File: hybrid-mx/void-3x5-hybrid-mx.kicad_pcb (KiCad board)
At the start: 2 copper layers, 140.5 x 112.5 mm, 81 parts, among them J1 Conn_01x02, J2 Conn_01x03_MountingPin, J3 Conn_01x02

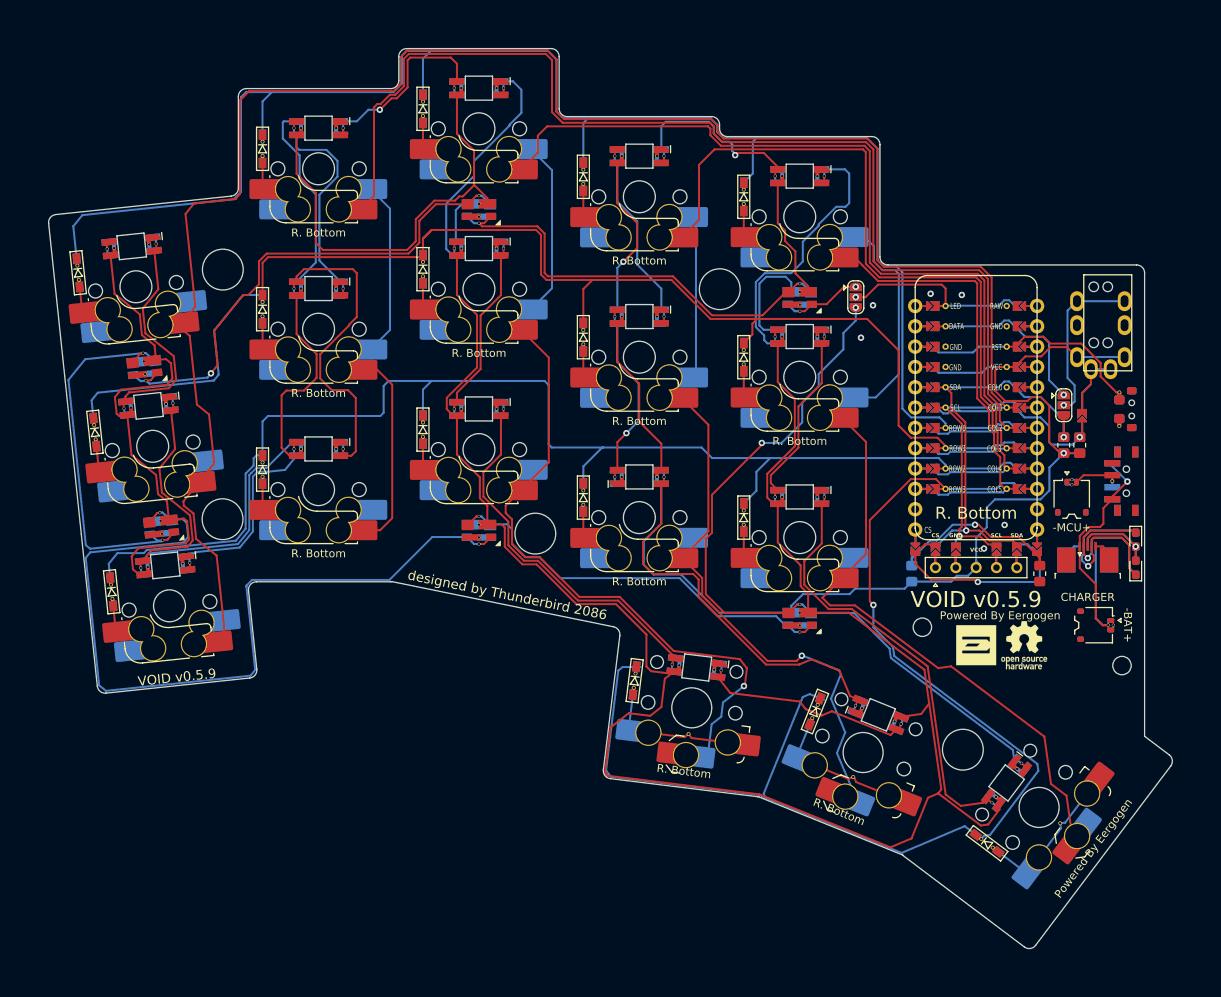
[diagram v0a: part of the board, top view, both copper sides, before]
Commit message: usb-c mod for hybrid
* updated
  - submodule
  - ergogen yaml
  - schematic and pcb
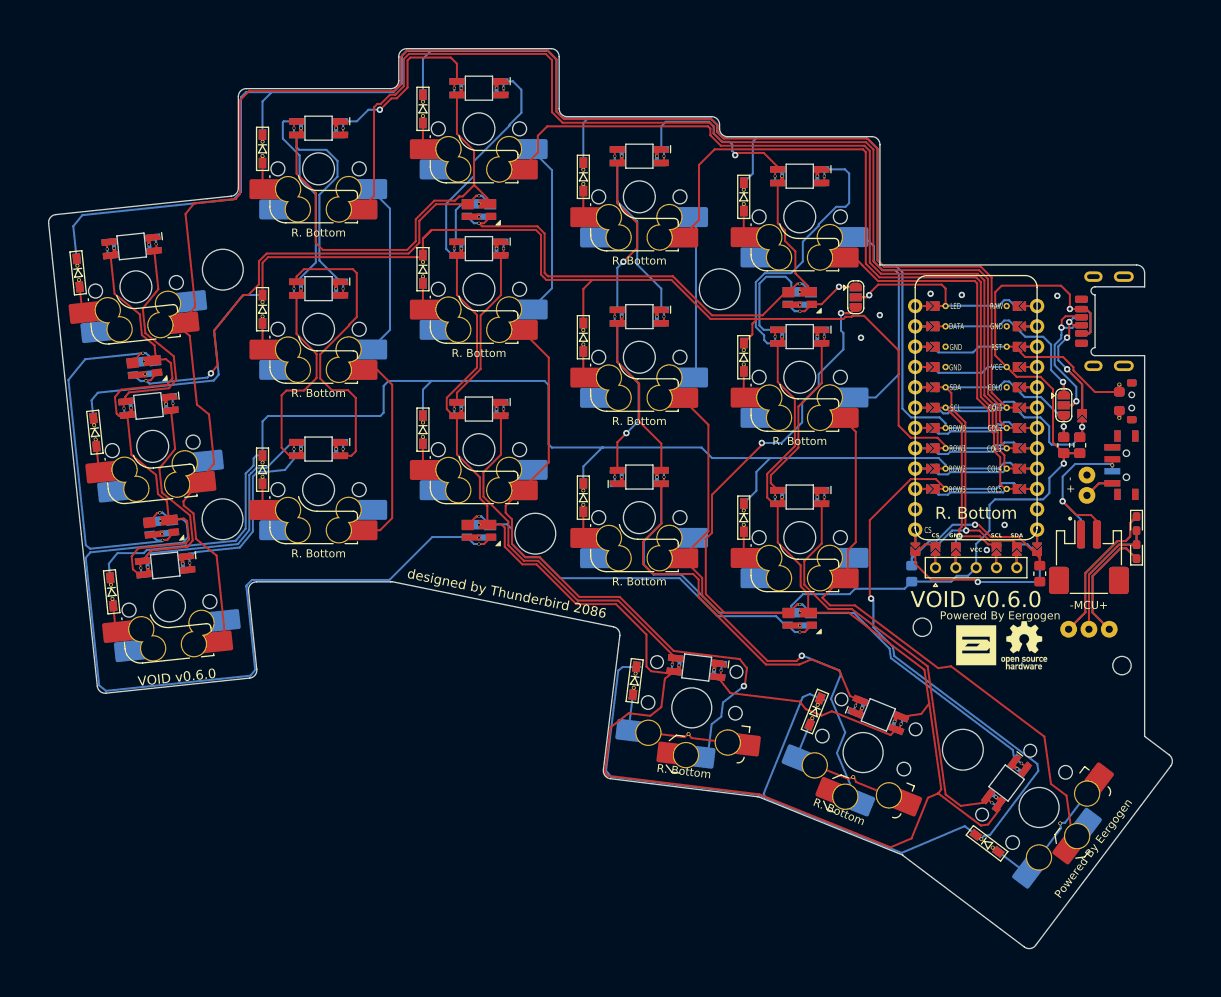
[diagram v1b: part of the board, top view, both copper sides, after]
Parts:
- removed TRRS1: MJ-4PP-9, TB2086_MISC:TRRS-PJ-320A-rev
- added J4: Conn_01x03, TB2086_MISC:Pogopin_1x03_P2.54mm, F.Cu at (210.9, 112.9)
- added SW_SPDT2: SW_SPDT2, TB2086_SMD:SW_SPDT_PCM12, F.Cu at (215.3, 92.4)
- J1: value Conn_01x02 -> USB_C_Receptacle_PowerOnly_6P; footprint TB2086_MISC:Molex_Pico-EZmate_78171-0002_1x02-1MP_P1.20mm_Vertical_rev -> TB2086_SMD:USB-20C-F-6C16_rev
- J2: value Conn_01x03_MountingPin -> Conn_01x02; footprint TB2086_MISC:TE_0-1734839-5_1x05-1MP_P0.5mm_Horizontal-rev -> TB2086_SMD:JST_PH_S2B-PH-SM4-TB_1x02-1MP_P2.00mm_Horizontal_rev
- J3: footprint TB2086_MISC:Molex_Pico-EZmate_78171-0002_1x02-1MP_P1.20mm_Vertical_rev -> TB2086_MISC:Pogopin_1x02_P2.54mm; moved to F.Cu
- L19, L20, L21, L22, L23, L24: footprint LED_SK6812MINI_PLCC4_3.5x3.5mm_P1.75mm_rev_all -> TB2086_LED:LED_SK6812MINI_PLCC4_3.5x3.5mm_P1.75mm_rev_all; moved to F.Cu
- LED1, LED2, LED3, LED4: footprint TB2086_SMD:LED_0603_1608Metric_Pad1.05x0.95mm_HandSolder -> TB2086_LED:LED_0603_1608Metric_Pad1.05x0.95mm_HandSolder
- R1: footprint R_0805_2012Metric_Pad1.20x1.40mm_HandSolder -> Resistor_SMD:R_0805_2012Metric_Pad1.20x1.40mm_HandSolder; moved to B.Cu
- R2: footprint R_0805_2012Metric_Pad1.20x1.40mm_HandSolder -> Resistor_SMD:R_0805_2012Metric_Pad1.20x1.40mm_HandSolder
- S16, S17: value SW_MX_HS -> SW_CHOC_HS
- S18: value SW_MX_HS -> SW_CHOC_HS; footprint TB2086_KEYSWITCH:SW_choc_v1_v2_HS_1.5u_reversible -> TB2086_KEYSWITCH:SW_choc_v1_v2_HS_1u_reversible
- SW_SPDT1: value SW_SPDT -> SW_SPDT1; footprint TB2086_SMD:SW_SPDT_PCM12_reversible -> TB2086_SMD:SW_SPDT_PCM12
- moved J1 22.7 mm to (214.5, 74.4), turned to 90 degrees
- moved J3 17.5 mm to (210.7, 94.9), turned to -90 degrees
- moved LED1 5.49 mm to (216.9, 99.7), turned to -90 degrees
- moved LED3 2.00 mm to (216.9, 103.2), turned to 90 degrees
- moved LED2 2.00 mm to (216.9, 99.7)
- moved SW_SPDT1 1.99 mm to (215.3, 92.4)
- moved LED4 1.51 mm to (216.9, 103.2)
- moved RSW1 0.99 mm to (216.3, 84.4)
- moved J2 0.15 mm to (210.9, 103.9)
- turned L19 to 0 degrees
- turned L23 to 0 degrees
- turned L24 to 0 degrees
- turned L20 to 0 degrees
- turned L21 to 6 degrees
- turned L22 to 6 degrees
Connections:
- J2 pad 1: BAT -> GND
- JP2 pad 2: Net-(JP2-C) -> Net-(J1-CC2)
- JP3 pad 2: Net-(JP3-B) -> Net-(J1-CC1)
- LED1 pad 1: Net-(J2-Pin_4) -> Net-(J4-Pin_1)
- LED1 pad 2: Net-(J2-Pin_3) -> Net-(J4-Pin_2)
- LED2 pad 1: Net-(J2-Pin_4) -> Net-(J4-Pin_1)
- LED2 pad 2: Net-(J2-Pin_3) -> Net-(J4-Pin_2)
- LED3 pad 1: Net-(J2-Pin_2) -> Net-(J4-Pin_3)
- LED3 pad 2: Net-(J2-Pin_3) -> Net-(J4-Pin_2)
- LED4 pad 1: Net-(J2-Pin_2) -> Net-(J4-Pin_3)
- LED4 pad 2: Net-(J2-Pin_3) -> Net-(J4-Pin_2)
- RSW1 pad MP: (no net) -> GND
- SW_SPDT1 pad 2: Net-(J1-Pin_2) -> Net-(J2-Pin_2)
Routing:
- net Net-(J4-Pin_1): track 0.00 -> 36.4 mm
- net Net-(J4-Pin_2): track 0.00 -> 32.2 mm
- net Net-(J4-Pin_3): track 0.00 -> 30.0 mm
- net BAT: track 37.1 -> 7.60 mm, vias 1 -> 0
- net Net-(J2-Pin_4): track 23.9 -> 0.00 mm, vias 1 -> 0
- net Net-(J1-CC1): track 0.00 -> 22.2 mm, vias 0 -> 3
- net Net-(JP2-C): track 20.9 -> 0.00 mm, vias 1 -> 0
- net Net-(J1-CC2): track 0.00 -> 20.5 mm, vias 0 -> 2
- net Net-(J2-Pin_3): track 19.3 -> 0.00 mm, vias 1 -> 0
- net VCC: track 627.1 -> 642.9 mm, vias 2 -> 3
- net Net-(JP3-B): track 13.8 -> 0.00 mm
- net GND: track 5.73 -> 0.00 mm, vias 6 -> 7
- net Net-(J1-Pin_2): track 4.83 -> 0.00 mm
- net LED_PER_KEY: track 93.4 -> 96.5 mm
- net LED_UNDERGLOW: track 10.1 -> 12.2 mm
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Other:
- outline, holes or cut-outs redrawn
- board text added: "- +"
- board text added: "VOID v0.6.0"
- board text removed: "-BAT+"
- board text removed: "CHARGER"
- board text removed: "VOID v0.5.9"

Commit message: updated choc
* fixed corner
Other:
- outline, holes or cut-outs redrawn
- board text added: "This corner was manually created."
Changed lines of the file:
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@@
 		(fp_arc
 			(start 4.085176 -6.75022)
-			(mid 5.499389 -6.164434)
+			(mid 5.499392 -6.164435)
 			(end 6.085176 -4.75022)
 			(stroke
@@
 		(fp_arc
 			(start 4.085176 -6.75022)
-			(mid 5.499389 -6.164434)
+			(mid 5.499392 -6.164435)
 			(end 6.085176 -4.75022)
 			(stroke
@@
 		)
 		(pad "1" thru_hole circle
-			(at -2.200002 0 353)
+			(at -2.200003 0 353)
 			(size 0.4 0.4)
 			(drill 0.3)
@@
 		)
 		(pad "3" thru_hole circle
-			(at 2.200002 0 353)
+			(at 2.200003 0 353)
 			(size 0.4 0.4)
 			(drill 0.3)
@@
 		(fp_arc
 			(start 4.085176 -6.75022)
-			(mid 5.499389 -6.164434)
+			(mid 5.499392 -6.164435)
 			(end 6.085176 -4.75022)
 			(stroke
@@
 		(fp_arc
 			(start 4.085176 -6.75022)
-			(mid 5.499389 -6.164434)
+			(mid 5.499392 -6.164435)
 			(end 6.085176 -4.75022)
 			(stroke
@@
 		(fp_arc
 			(start 4.085176 -6.75022)
-			(mid 5.499389 -6.164434)
+			(mid 5.499392 -6.164435)
 			(end 6.085176 -4.75022)
 			(stroke
@@
 		(fp_arc
 			(start 4.085176 -6.75022)
-			(mid 5.499389 -6.164434)
+			(mid 5.499392 -6.164435)
 			(end 6.085176 -4.75022)
 			(stroke
@@
 		(fp_arc
 			(start 4.085176 -6.75022)
-			(mid 5.499389 -6.164434)
+			(mid 5.499392 -6.164435)
 			(end 6.085176 -4.75022)
 			(stroke
@@
 		(fp_arc
 			(start 4.085176 -6.75022)
-			(mid 5.499389 -6.164434)
+			(mid 5.499392 -6.164435)
 			(end 6.085176 -4.75022)
 			(stroke
@@
 		(tags "resistor handsolder")
 		(property "Reference" "R2"
-			(at 0 -1.65 270)
+			(at 0 -1.65 -90)
 			(layer "F.SilkS")
 			(hide yes)
@@
 		(fp_arc
 			(start 4.085176 -6.75022)
-			(mid 5.499389 -6.164434)
+			(mid 5.499392 -6.164435)
 			(end 6.085176 -4.75022)
 			(stroke
@@
 		(fp_arc
 			(start 4.085176 -6.75022)
-			(mid 5.499389 -6.164434)
+			(mid 5.499392 -6.164435)
 			(end 6.085176 -4.75022)
 			(stroke
@@
 		(fp_arc
 			(start 4.085176 -6.75022)
-			(mid 5.499389 -6.164434)
+			(mid 5.499392 -6.164435)
 			(end 6.085176 -4.75022)
 			(stroke
@@
 		(fp_arc
 			(start 4.085176 -6.75022)
-			(mid 5.499389 -6.164434)
+			(mid 5.499392 -6.164435)
 			(end 6.085176 -4.75022)
 			(stroke
@@
 		(fp_arc
 			(start -2.444146 -0.85)
-			(mid -1.620516 -2.173416)
+			(mid -1.620517 -2.173415)
 			(end -0.149824 -2.69)
 			(stroke
@@
 		(fp_arc
 			(start 4.085176 -6.75022)
-			(mid 5.499389 -6.164435)
+			(mid 5.499392 -6.164435)
 			(end 6.085176 -4.75022)
 			(stroke
@@
 		(fp_line
 			(start 7.465 -6.31)
-			(end 4.915002 -6.31)
+			(end 4.915003 -6.31)
 			(stroke
 				(width 0.05)
@@
 		(fp_line
 			(start 4.915 -6.74)
-			(end 4.915002 -6.31)
+			(end 4.915003 -6.31)
 			(stroke
 				(width 0.05)
@@
 		(fp_arc
 			(start 4.085176 -6.75022)
-			(mid 5.499389 -6.164435)
+			(mid 5.499392 -6.164435)
 			(end 6.085176 -4.75022)
 			(stroke
@@
 		(fp_arc
 			(start 4.085176 -6.75022)
-			(mid 5.499389 -6.164434)
+			(mid 5.499392 -6.164435)
 			(end 6.085176 -4.75022)
 			(stroke
@@
 		(fp_arc
 			(start 4.085176 -6.75022)
-			(mid 5.499389 -6.164434)
+			(mid 5.499392 -6.164435)
 			(end 6.085176 -4.75022)
 			(stroke
@@
 		(fp_arc
 			(start 4.085176 -6.75022)
-			(mid 5.499389 -6.164434)
+			(mid 5.499392 -6.164435)
 			(end 6.085176 -4.75022)
 			(stroke
@@
 		(fp_arc
 			(start 4.085176 -6.75022)
-			(mid 5.499389 -6.164434)
+			(mid 5.499392 -6.164435)
 			(end 6.085176 -4.75022)
 			(stroke
@@
 		(fp_arc
 			(start -3.4 1.475)
-			(mid -2.826424 1.655849)
+			(mid -2.826425 1.655849)
 			(end -2.460307 2.13298)
 			(stroke
@@
 		(fp_arc
 			(start -0.299999 3.624999)
-			(mid -1.577272 3.167235)
+			(mid -1.577271 3.167235)
 			(end -2.455444 2.13293)
 			(stroke
@@
 		(fp_arc
 			(start 2.455444 2.13293)
-			(mid 1.577273 3.167237)
+			(mid 1.577274 3.167237)
 			(end 0.299999 3.624997)
 			(stroke
@@
 		(at 154.701652 93.836424 180)
 		(property "Reference" "L10"
-			(at 0 2.1 360)
+			(at 0 2.1 0)
 			(layer "Eco1.User")
 			(effects
@@
 		)
 		(property "Value" "SK6812MINI-E"
-			(at 0 -0.5 360)
+			(at 0 -0.5 0)
 			(layer "B.SilkS")
 			(hide yes)
@@
 		)
 		(property "Footprint" "TB2086_LED:LED_SK6812MINI-E_rev"
-			(at 0 0 360)
+			(at 0 0 0)
 			(layer "F.Fab")
 			(hide yes)
@@
 		)
 		(property "Datasheet" "https://cdn-shop.adafruit.com/product-files/2686/SK6812MINI_REV.01-1-2.pdf"
-			(at 0 0 360)
+			(at 0 0 0)
 			(layer "F.Fab")
 			(hide yes)
@@
 		)
 		(property "Description" ""
-			(at 0 0 360)
+			(at 0 0 0)
 			(layer "F.Fab")
 			(hide yes)
@@
 		(fp_arc
 			(start 4.085176 -6.75022)
-			(mid 5.499389 -6.164434)
+			(mid 5.499392 -6.164435)
 			(end 6.085176 -4.75022)
 			(stroke
@@
 		(fp_arc
 			(start 4.085176 -6.75022)
-			(mid 5.499389 -6.164434)
+			(mid 5.499392 -6.164435)
 			(end 6.085176 -4.75022)
 			(stroke
@@
 		(fp_arc
 			(start -2.444146 -0.85)
-			(mid -1.620516 -2.173416)
+			(mid -1.620517 -2.173415)
 			(end -0.149824 -2.69)
 			(stroke
@@
 		(fp_arc
 			(start 4.085176 -6.75022)
-			(mid 5.499389 -6.164435)
+			(mid 5.499392 -6.164435)
 			(end 6.085176 -4.75022)
 			(stroke
@@
 		(fp_line
 			(start 7.465 -6.31)
-			(end 4.915002 -6.31)
+			(end 4.915003 -6.31)
 			(stroke
 				(width 0.05)
@@
 		(fp_line
 			(start 4.915 -6.74)
-			(end 4.915002 -6.31)
+			(end 4.915003 -6.31)
 			(stroke
 				(width 0.05)
@@
 		(fp_arc
 			(start 4.085176 -6.75022)
-			(mid 5.499389 -6.164435)
+			(mid 5.499392 -6.164435)
 			(end 6.085176 -4.75022)
 			(stroke
@@
 		(fp_arc
 			(start 4.085176 -6.75022)
-			(mid 5.499389 -6.164434)
+			(mid 5.499392 -6.164435)
 			(end 6.085176 -4.75022)
 			(stroke
@@
 		(fp_arc
 			(start 4.085176 -6.75022)
-			(mid 5.499389 -6.164434)
+			(mid 5.499392 -6.164435)
 			(end 6.085176 -4.75022)
 			(stroke
@@
 		(fp_arc
 			(start 4.085176 -6.75022)
-			(mid 5.499389 -6.164434)
+			(mid 5.499392 -6.164435)
 			(end 6.085176 -4.75022)
 			(stroke
@@
 		(fp_arc
 			(start 4.085176 -6.75022)
-			(mid 5.499389 -6.164434)
+			(mid 5.499392 -6.164435)
 			(end 6.085176 -4.75022)
 			(stroke
@@
 		(fp_arc
 			(start 4.085176 -6.75022)
-			(mid 5.499389 -6.164434)
+			(mid 5.499392 -6.164435)
 			(end 6.085176 -4.75022)
 			(stroke
@@
 		(fp_arc
 			(start 4.085176 -6.75022)
-			(mid 5.499389 -6.164434)
+			(mid 5.499392 -6.164435)
 			(end 6.085176 -4.75022)
 			(stroke
@@
 		(fp_arc
 			(start -6.95 -6.45)
-			(mid -6.803553 -6.803552)
+			(mid -6.803552 -6.803552)
 			(end -6.45 -6.95)
 			(stroke
@@
 		(fp_arc
 			(start -6.45 6.95)
-			(mid -6.803552 6.803553)
+			(mid -6.803552 6.803552)
 			(end -6.95 6.45)
 			(stroke
@@
 		(fp_arc
 			(start -3.45 6.125001)
-			(mid -2.742894 6.417893)
+			(mid -2.742893 6.417893)
 			(end -2.45 7.125)
 			(stroke
@@
 		(fp_arc
 			(start -2.444146 -0.85)
-			(mid -1.620516 -2.173416)
+			(mid -1.620517 -2.173415)
 			(end -0.149824 -2.69)
 			(stroke
@@
 		(fp_arc
 			(start 4.085176 -6.75022)
-			(mid 5.499389 -6.164435)
+			(mid 5.499392 -6.164435)
 			(end 6.085176 -4.75022)
 			(stroke
@@
 		(fp_line
 			(start 7.465 -6.31)
-			(end 4.915002 -6.31)
+			(end 4.915003 -6.31)
 			(stroke
 				(width 0.05)
@@
 		(fp_line
 			(start 4.915 -6.74)
-			(end 4.915002 -6.31)
+			(end 4.915003 -6.31)
 			(stroke
 				(width 0.05)
@@
 		(fp_arc
 			(start 4.085176 -6.75022)
-			(mid 5.499389 -6.164435)
+			(mid 5.499392 -6.164435)
 			(end 6.085176 -4.75022)
 			(stroke
@@
 	(gr_line
 		(start 216.859152 67.331424)
-		(end 184.776652 67.331424)
+		(end 186.122009 67.324289)
 		(stroke
 			(width 0.15)
@@
 		(layer "Edge.Cuts")
 	)
+	(gr_arc
+		(start 186.122009 67.324289)
+		(mid 185.17 66.93)
+		(end 184.775711 65.977991)
+		(stroke
+			(width 0.15)
+			(type default)
+		)
+		(layer "Edge.Cuts")
+	)
 	(gr_circle
 		(center 102.601652 99.116424)
@@
 	)
 	(gr_line
-		(start 184.776652 67.331424)
+		(start 184.775711 65.977991)
 		(end 184.776652 52.291424)
 		(stroke
@@
 		)
 	)
+	(gr_text "This corner was manually created. "
+		(at 185.45 66.63 0)
+		(layer "Cmts.User")
+		(effects
+			(font
+				(size 1 1)
+				(thickness 0.15)
+			)
+			(justify left bottom)
+		)
+	)

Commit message: updated PCBs
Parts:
- moved D8 5.70 mm to (133.1, 69.6)
- moved D9 5.70 mm to (133.1, 49.5)
- moved D2 5.70 mm to (92.1, 89.9)
- moved D7 5.70 mm to (133.1, 89.6)
- moved D11 5.70 mm to (153.1, 78.1)
- moved D14 5.70 mm to (173.2, 80.6)
- moved D16 5.70 mm to (159.6, 121.0)
- moved D17 5.70 mm to (182.1, 124.8)
- moved D18 5.70 mm to (203.6, 141.3)
- moved D3 5.70 mm to (90.0, 70.0)
- moved D5 5.70 mm to (113.0, 74.6)
- moved J1 5.70 mm to (219.9, 76.1)
- moved J2 5.70 mm to (216.3, 105.6)
- moved J3 5.70 mm to (216.1, 96.6)
- moved J4 5.70 mm to (216.3, 114.6)
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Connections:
- RSW1 pad MP: GND -> (no net)
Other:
- outline, holes or cut-outs redrawn
- board text added: "Powered By Ergogen"
- board text added: "offset: 90, 70 from origin"
- board text removed: "Powered By Eergogen"
- board text removed: "This corner was manually created."
